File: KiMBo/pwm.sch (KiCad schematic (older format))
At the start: 3 parts, among them U26 PCA9685

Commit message: Create more footprints and add more associations
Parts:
- U26: footprint (none) -> Housings_SSOP:TSSOP-28_4.4x9.7mm_Pitch0.65mm
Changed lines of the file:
@@
 F 0 "U26" H 5450 4587 60  0000 C CNN
 F 1 "PCA9685" H 5450 4481 60  0000 C CNN
-F 2 "" H 5450 3600 60  0001 C CNN
+F 2 "Housings_SSOP:TSSOP-28_4.4x9.7mm_Pitch0.65mm" H 5450 3600 60  0001 C CNN
 F 3 "" H 5450 3600 60  0000 C CNN
 	1    5450 3600

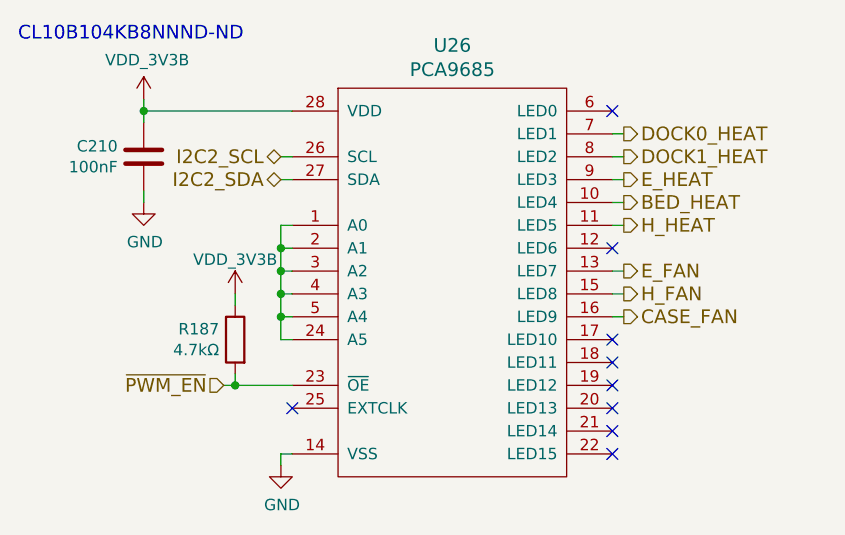
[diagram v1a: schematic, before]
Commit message: Add more footprints and more associations, one association left!
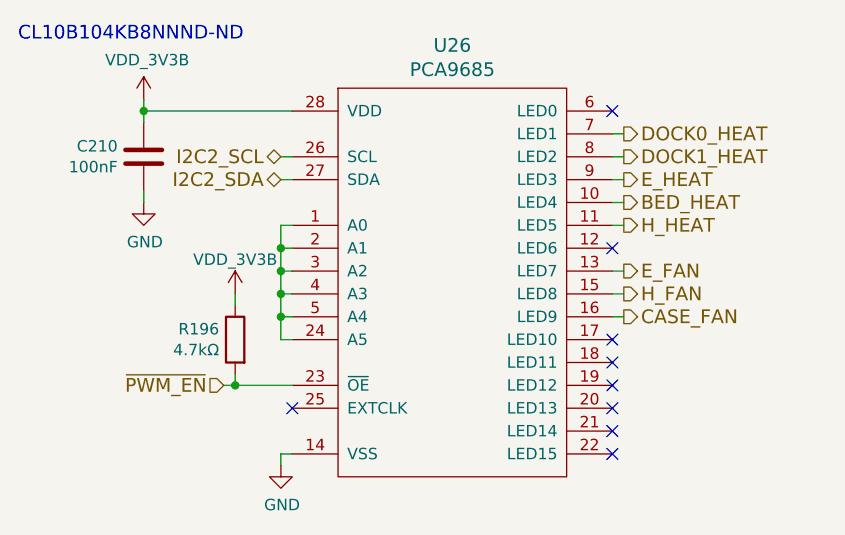
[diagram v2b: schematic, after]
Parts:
- renumbered R187 to R196
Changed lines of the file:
@@
 $EndComp
 $Comp
-L GND #PWR0259
+L GND #PWR0261
 U 1 1 595584AE
 P 4100 3300
-F 0 "#PWR0259" H 4100 3050 50  0001 C CNN
+F 0 "#PWR0261" H 4100 3050 50  0001 C CNN
 F 1 "GND" H 4105 3127 50  0000 C CNN
 F 2 "" H 4100 3300 50  0000 C CNN
@@
 	4450 4100 4750 4100
 $Comp
-L GND #PWR0260
+L GND #PWR0262
 U 1 1 595593D7
 P 4700 4450
-F 0 "#PWR0260" H 4700 4200 50  0001 C CNN
+F 0 "#PWR0262" H 4700 4200 50  0001 C CNN
 F 1 "GND" H 4705 4277 50  0000 C CNN
 F 2 "" H 4700 4450 50  0000 C CNN
@@
 ~PWM_EN
 $Comp
-L R R187
+L R R196
 U 1 1 5970A901
 P 4500 3900
-F 0 "R187" H 4570 3946 50  0000 L CNN
+F 0 "R196" H 4570 3946 50  0000 L CNN
 F 1 "4.7kΩ" H 4570 3855 50  0000 L CNN
 F 2 "Resistors_SMD:R_0603" V 4430 3900 50  0001 C CNN
@@
 DOCK1_HEAT
 $Comp
-L VDD_3V3B #PWR0261
+L VDD_3V3B #PWR0263
 U 1 1 5A115F67
 P 4500 3700
-F 0 "#PWR0261" H 4500 3550 50  0001 C CNN
+F 0 "#PWR0263" H 4500 3550 50  0001 C CNN
 F 1 "VDD_3V3B" H 4500 3850 50  0000 C CNN
 F 2 "" H 4500 3700 50  0000 C CNN
@@
 $EndComp
 $Comp
-L VDD_3V3B #PWR0262
+L VDD_3V3B #PWR0264
 U 1 1 5A118229
 P 4100 2850
-F 0 "#PWR0262" H 4100 2700 50  0001 C CNN
+F 0 "#PWR0264" H 4100 2700 50  0001 C CNN
 F 1 "VDD_3V3B" H 4115 3023 50  0000 C CNN
 F 2 "" H 4100 2850 50  0000 C CNN

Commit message: Begin layout
Arrange all connectors to get a feel for the area.
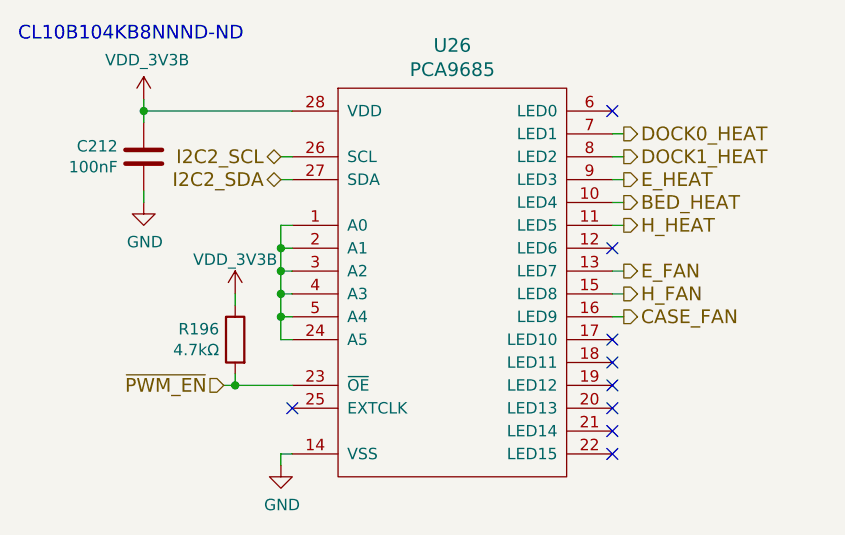
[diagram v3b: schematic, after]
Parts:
- renumbered C210 to C212
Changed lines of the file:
@@
 $EndComp
 $Comp
-L C C210
+L C C212
 U 1 1 59558467
 P 4100 3100
-F 0 "C210" H 4214 3146 50  0000 L CNN
+F 0 "C212" H 4214 3146 50  0000 L CNN
 F 1 "100nF" H 4214 3055 50  0000 L CNN
 F 2 "Capacitors_SMD:C_0603" H 4138 2950 50  0001 C CNN
@@
 $EndComp
 $Comp
-L GND #PWR0261
+L GND #PWR0264
 U 1 1 595584AE
 P 4100 3300
-F 0 "#PWR0261" H 4100 3050 50  0001 C CNN
+F 0 "#PWR0264" H 4100 3050 50  0001 C CNN
 F 1 "GND" H 4105 3127 50  0000 C CNN
 F 2 "" H 4100 3300 50  0000 C CNN
@@
 	4450 4100 4750 4100
 $Comp
-L GND #PWR0262
+L GND #PWR0265
 U 1 1 595593D7
 P 4700 4450
-F 0 "#PWR0262" H 4700 4200 50  0001 C CNN
+F 0 "#PWR0265" H 4700 4200 50  0001 C CNN
 F 1 "GND" H 4705 4277 50  0000 C CNN
 F 2 "" H 4700 4450 50  0000 C CNN
@@
 DOCK1_HEAT
 $Comp
-L VDD_3V3B #PWR0263
+L VDD_3V3B #PWR0266
 U 1 1 5A115F67
 P 4500 3700
-F 0 "#PWR0263" H 4500 3550 50  0001 C CNN
+F 0 "#PWR0266" H 4500 3550 50  0001 C CNN
 F 1 "VDD_3V3B" H 4500 3850 50  0000 C CNN
 F 2 "" H 4500 3700 50  0000 C CNN
@@
 $EndComp
 $Comp
-L VDD_3V3B #PWR0264
+L VDD_3V3B #PWR0267
 U 1 1 5A118229
 P 4100 2850
-F 0 "#PWR0264" H 4100 2700 50  0001 C CNN
+F 0 "#PWR0267" H 4100 2700 50  0001 C CNN
 F 1 "VDD_3V3B" H 4115 3023 50  0000 C CNN
 F 2 "" H 4100 2850 50  0000 C CNN

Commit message: Remove HDMI from the schematic
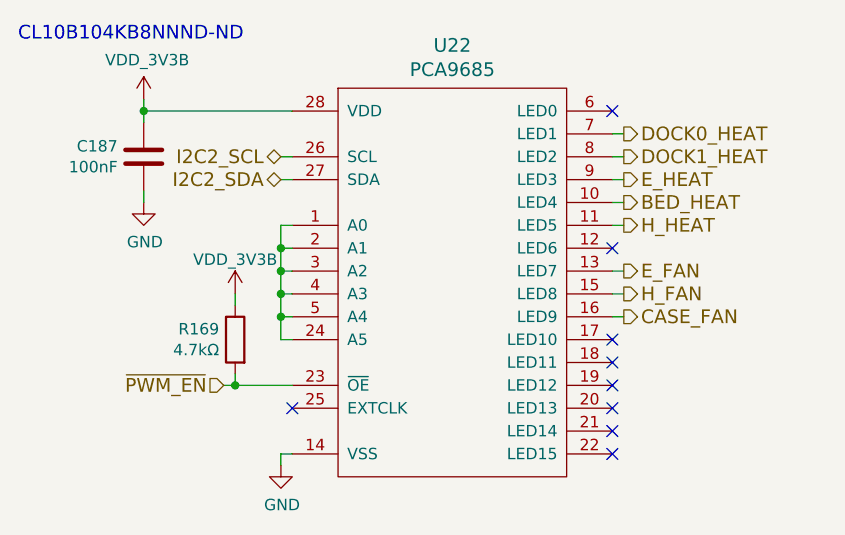
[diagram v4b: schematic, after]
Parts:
- renumbered C212 to C187, R196 to R169, U26 to U22
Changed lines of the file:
@@
 $Descr A4 11693 8268
 encoding utf-8
-Sheet 24 26
+Sheet 24 25
 Title ""
 Date ""
@@
 $EndDescr
 $Comp
-L PCA9685 U26
+L PCA9685 U22
 U 1 1 595289D2
 P 5450 3600
-F 0 "U26" H 5450 4587 60  0000 C CNN
+F 0 "U22" H 5450 4587 60  0000 C CNN
 F 1 "PCA9685" H 5450 4481 60  0000 C CNN
 F 2 "Housings_SSOP:TSSOP-28_4.4x9.7mm_Pitch0.65mm" H 5450 3600 60  0001 C CNN
@@
 $EndComp
 $Comp
-L C C212
+L C C187
 U 1 1 59558467
 P 4100 3100
-F 0 "C212" H 4214 3146 50  0000 L CNN
+F 0 "C187" H 4214 3146 50  0000 L CNN
 F 1 "100nF" H 4214 3055 50  0000 L CNN
 F 2 "Capacitors_SMD:C_0603" H 4138 2950 50  0001 C CNN
@@
 $EndComp
 $Comp
-L GND #PWR0264
+L GND #PWR0233
 U 1 1 595584AE
 P 4100 3300
-F 0 "#PWR0264" H 4100 3050 50  0001 C CNN
+F 0 "#PWR0233" H 4100 3050 50  0001 C CNN
 F 1 "GND" H 4105 3127 50  0000 C CNN
 F 2 "" H 4100 3300 50  0000 C CNN
@@
 	4450 4100 4750 4100
 $Comp
-L GND #PWR0265
+L GND #PWR0234
 U 1 1 595593D7
 P 4700 4450
-F 0 "#PWR0265" H 4700 4200 50  0001 C CNN
+F 0 "#PWR0234" H 4700 4200 50  0001 C CNN
 F 1 "GND" H 4705 4277 50  0000 C CNN
 F 2 "" H 4700 4450 50  0000 C CNN
@@
 ~PWM_EN
 $Comp
-L R R196
+L R R169
 U 1 1 5970A901
 P 4500 3900
-F 0 "R196" H 4570 3946 50  0000 L CNN
+F 0 "R169" H 4570 3946 50  0000 L CNN
 F 1 "4.7kΩ" H 4570 3855 50  0000 L CNN
 F 2 "Resistors_SMD:R_0603" V 4430 3900 50  0001 C CNN
@@
 DOCK1_HEAT
 $Comp
-L VDD_3V3B #PWR0266
+L VDD_3V3B #PWR0235
 U 1 1 5A115F67
 P 4500 3700
-F 0 "#PWR0266" H 4500 3550 50  0001 C CNN
+F 0 "#PWR0235" H 4500 3550 50  0001 C CNN
 F 1 "VDD_3V3B" H 4500 3850 50  0000 C CNN
 F 2 "" H 4500 3700 50  0000 C CNN
@@
 $EndComp
 $Comp
-L VDD_3V3B #PWR0267
+L VDD_3V3B #PWR0236
 U 1 1 5A118229
 P 4100 2850
-F 0 "#PWR0267" H 4100 2700 50  0001 C CNN
+F 0 "#PWR0236" H 4100 2700 50  0001 C CNN
 F 1 "VDD_3V3B" H 4115 3023 50  0000 C CNN
 F 2 "" H 4100 2850 50  0000 C CNN

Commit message: More stepper motor driver progress
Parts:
- renumbered R169 to R171
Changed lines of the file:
@@
 $Descr A4 11693 8268
 encoding utf-8
-Sheet 24 25
+Sheet 22 25
 Title ""
 Date ""
@@
 ~PWM_EN
 $Comp
-L R R169
+L R R171
 U 1 1 5970A901
 P 4500 3900
-F 0 "R169" H 4570 3946 50  0000 L CNN
+F 0 "R171" H 4570 3946 50  0000 L CNN
 F 1 "4.7kΩ" H 4570 3855 50  0000 L CNN
 F 2 "Resistors_SMD:R_0603" V 4430 3900 50  0001 C CNN

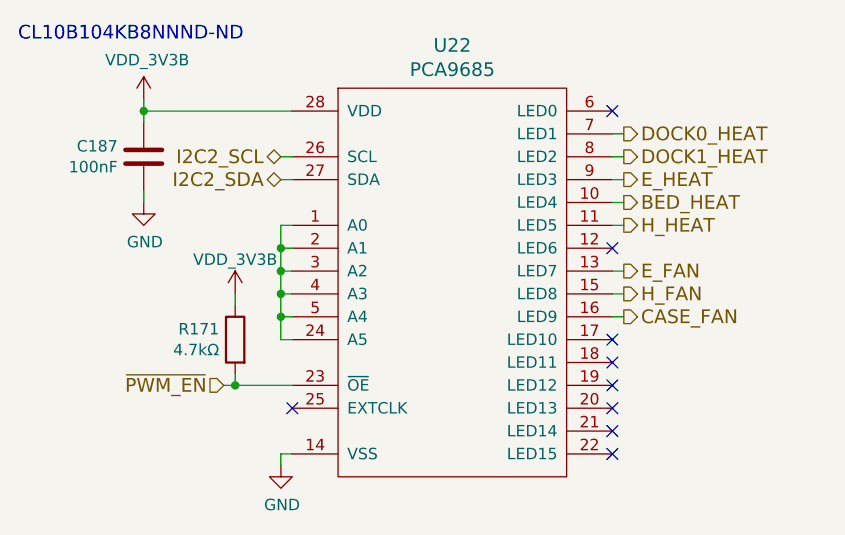
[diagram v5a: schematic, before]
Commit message: Begin laying out the bed heater circuit
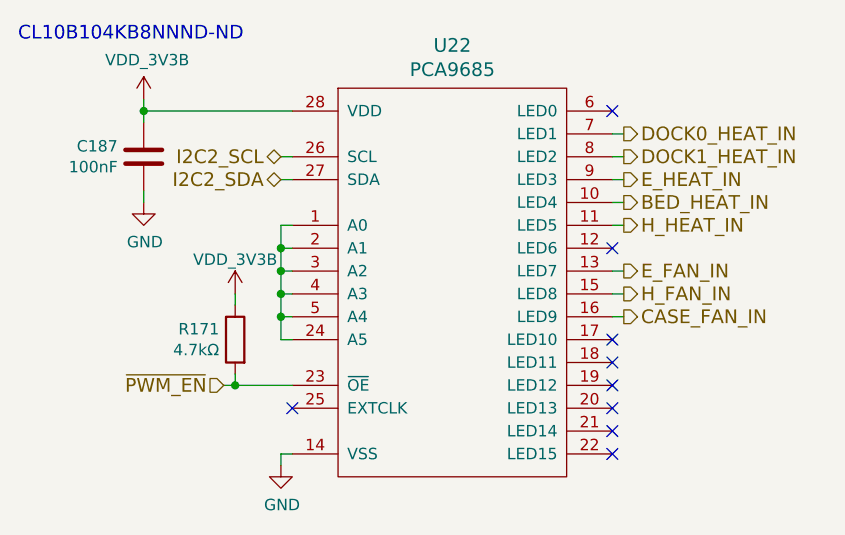
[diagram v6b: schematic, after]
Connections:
- net BED_HEAT renamed BED_HEAT_IN
- net CASE_FAN renamed CASE_FAN_IN
- net DOCK0_HEAT renamed DOCK0_HEAT_IN
- net DOCK1_HEAT renamed DOCK1_HEAT_IN
- net E_FAN renamed E_FAN_IN
- net E_HEAT renamed E_HEAT_IN
- net H_FAN renamed H_FAN_IN
- net H_HEAT renamed H_HEAT_IN
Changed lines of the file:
@@
 	6150 3800 6200 3800
 Text HLabel 6200 3200 2    60   Output ~ 0
-E_HEAT
+E_HEAT_IN
 Text HLabel 6200 3300 2    60   Output ~ 0
-BED_HEAT
+BED_HEAT_IN
 Text HLabel 6200 3400 2    60   Output ~ 0
-H_HEAT
+H_HEAT_IN
 Text HLabel 6200 3600 2    60   Output ~ 0
-E_FAN
+E_FAN_IN
 Text HLabel 6200 3700 2    60   Output ~ 0
-H_FAN
+H_FAN_IN
 Text HLabel 6200 3800 2    60   Output ~ 0
-CASE_FAN
+CASE_FAN_IN
 Text HLabel 4700 3100 0    60   BiDi ~ 0
 I2C2_SCL
@@
 	6150 3100 6200 3100
 Text HLabel 6200 3000 2    60   Output ~ 0
-DOCK0_HEAT
+DOCK0_HEAT_IN
 Text HLabel 6200 3100 2    60   Output ~ 0
-DOCK1_HEAT
+DOCK1_HEAT_IN
 $Comp
 L VDD_3V3B #PWR0235

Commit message: Daisy chain the SPI stepper motor driver interface, continue work on the E-heater layout
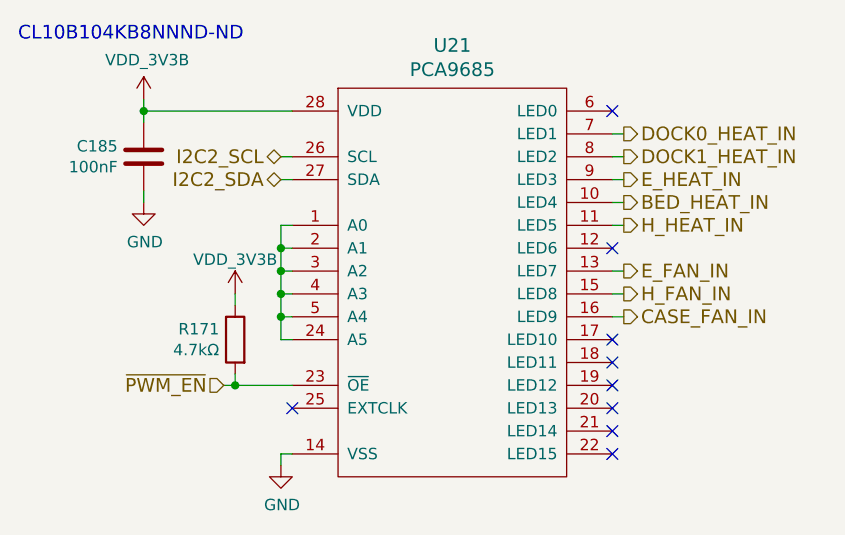
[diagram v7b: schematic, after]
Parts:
- renumbered C187 to C185, U22 to U21
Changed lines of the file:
@@
 $EndDescr
 $Comp
-L PCA9685 U22
+L PCA9685 U21
 U 1 1 595289D2
 P 5450 3600
-F 0 "U22" H 5450 4587 60  0000 C CNN
+F 0 "U21" H 5450 4587 60  0000 C CNN
 F 1 "PCA9685" H 5450 4481 60  0000 C CNN
 F 2 "Housings_SSOP:TSSOP-28_4.4x9.7mm_Pitch0.65mm" H 5450 3600 60  0001 C CNN
@@
 $EndComp
 $Comp
-L C C187
+L C C185
 U 1 1 59558467
 P 4100 3100
-F 0 "C187" H 4214 3146 50  0000 L CNN
+F 0 "C185" H 4214 3146 50  0000 L CNN
 F 1 "100nF" H 4214 3055 50  0000 L CNN
 F 2 "Capacitors_SMD:C_0603" H 4138 2950 50  0001 C CNN
@@
 $EndComp
 $Comp
-L GND #PWR0233
+L GND #PWR213
 U 1 1 595584AE
 P 4100 3300
-F 0 "#PWR0233" H 4100 3050 50  0001 C CNN
+F 0 "#PWR213" H 4100 3050 50  0001 C CNN
 F 1 "GND" H 4105 3127 50  0000 C CNN
 F 2 "" H 4100 3300 50  0000 C CNN
@@
 	4450 4100 4750 4100
 $Comp
-L GND #PWR0234
+L GND #PWR215
 U 1 1 595593D7
 P 4700 4450
-F 0 "#PWR0234" H 4700 4200 50  0001 C CNN
+F 0 "#PWR215" H 4700 4200 50  0001 C CNN
 F 1 "GND" H 4705 4277 50  0000 C CNN
 F 2 "" H 4700 4450 50  0000 C CNN
@@
 DOCK1_HEAT_IN
 $Comp
-L VDD_3V3B #PWR0235
+L VDD_3V3B #PWR214
 U 1 1 5A115F67
 P 4500 3700
-F 0 "#PWR0235" H 4500 3550 50  0001 C CNN
+F 0 "#PWR214" H 4500 3550 50  0001 C CNN
 F 1 "VDD_3V3B" H 4500 3850 50  0000 C CNN
 F 2 "" H 4500 3700 50  0000 C CNN
@@
 $EndComp
 $Comp
-L VDD_3V3B #PWR0236
+L VDD_3V3B #PWR212
 U 1 1 5A118229
 P 4100 2850
-F 0 "#PWR0236" H 4100 2700 50  0001 C CNN
+F 0 "#PWR212" H 4100 2700 50  0001 C CNN
 F 1 "VDD_3V3B" H 4115 3023 50  0000 C CNN
 F 2 "" H 4100 2850 50  0000 C CNN
